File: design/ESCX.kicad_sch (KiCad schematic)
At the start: 18 parts, among them J1 HALL_ENC, J4 SWD, J5 USB_OTG, SW1 SENSOR_VOLTAGE

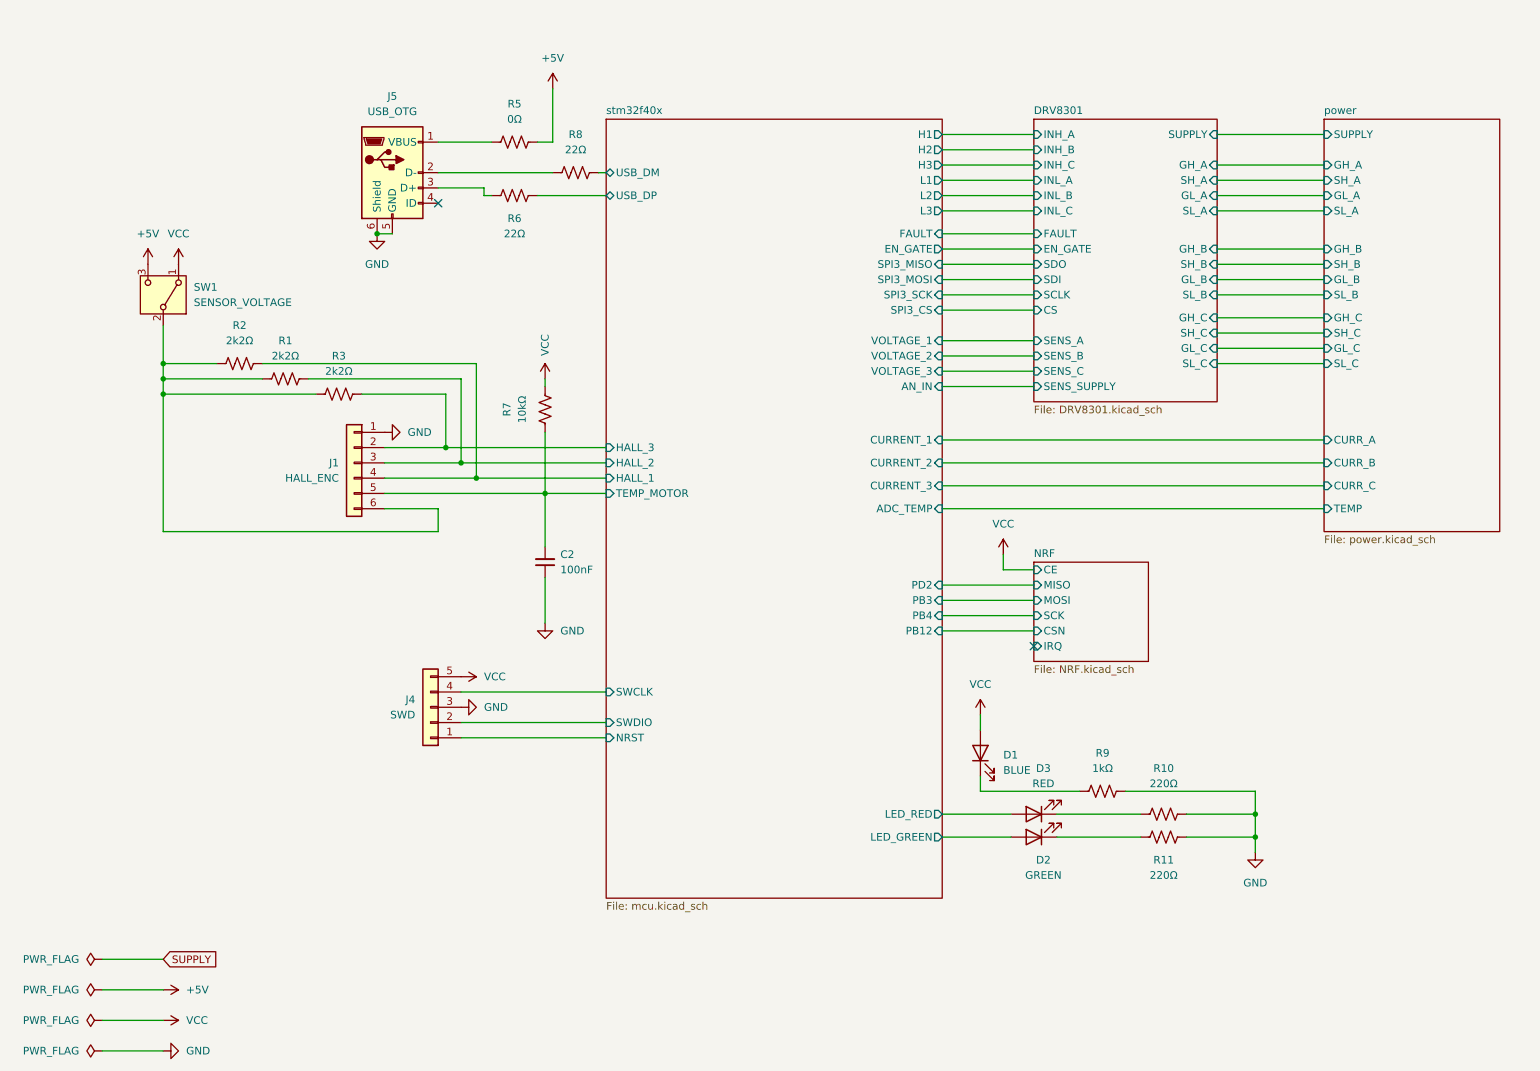
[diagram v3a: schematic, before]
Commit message: Cambios en el esquemático
- Cambio de Vcc por +3.3V
- Agregado de hoja para desarrollar la entrada de tensión alterna
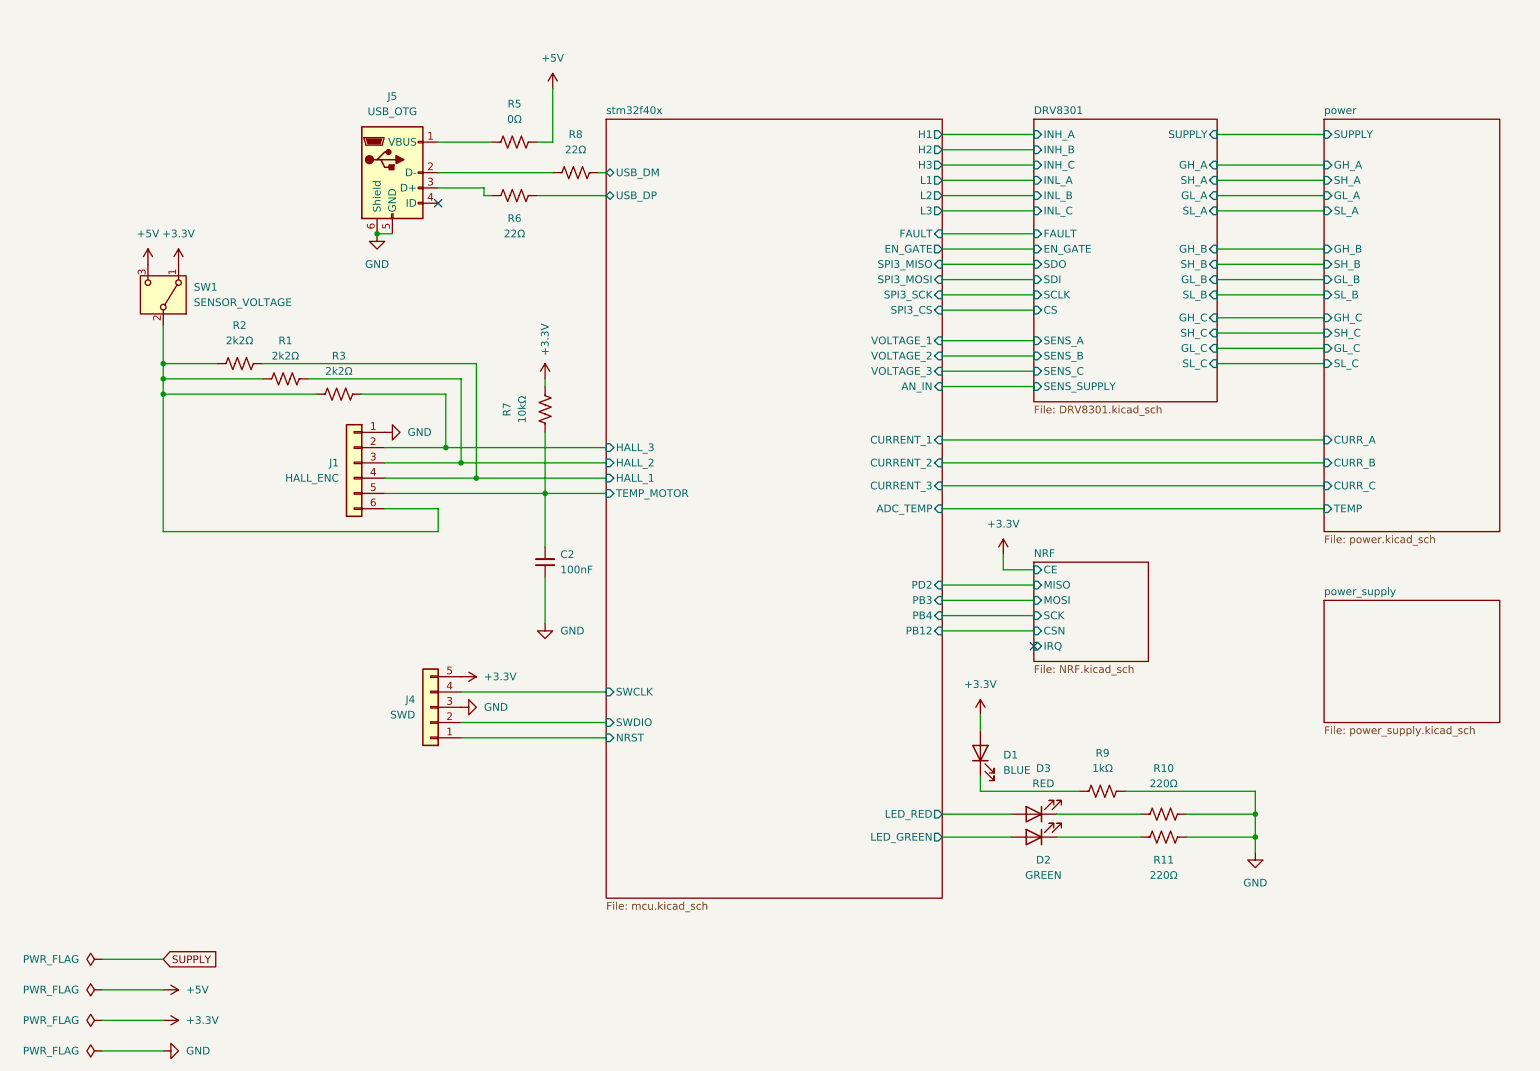
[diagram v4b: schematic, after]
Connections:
- net VCC renamed +3.3V
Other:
- added sheet power_supply (power_supply.kicad_sch)
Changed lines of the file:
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@@
 			)
 		)
-		(property "Value" "VCC"
+		(property "Value" "+3.3V"
 			(at 106.6799 72.39 90)
 			(effects
@@
 			)
 		)
-		(property "Value" "VCC"
+		(property "Value" "+3.3V"
 			(at 45.72 52.07 0)
 			(effects
@@
 			)
 		)
-		(property "Value" "VCC"
+		(property "Value" "+3.3V"
 			(at 46.99 182.8799 90)
 			(effects
@@
 			)
 		)
-		(property "Value" "VCC"
+		(property "Value" "+3.3V"
 			(at 96.52 125.7299 90)
 			(effects
@@
 			)
 		)
-		(property "Value" "VCC"
+		(property "Value" "+3.3V"
 			(at 179.07 127 0)
 			(effects
@@
 			)
 		)
-		(property "Value" "VCC"
+		(property "Value" "+3.3V"
 			(at 182.88 100.33 0)
 			(effects
@@
 				)
 			)
+		)
+	)
+	(sheet
+		(at 236.22 113.03)
+		(size 29.21 20.32)
+		(fields_autoplaced yes)
+		(stroke
+			(width 0.1524)
+			(type solid)
+		)
+		(fill
+			(color 0 0 0 0.0000)
+		)
+		(property "Sheetname" "power_supply"
+			(at 236.22 112.3184 0)
+			(effects
+				(font
+					(size 1.27 1.27)
+				)
+				(justify left bottom)
+			)
+		)
+		(property "Sheetfile" "power_supply.kicad_sch"
+			(at 236.22 133.9346 0)
+			(effects
+				(font
+					(size 1.27 1.27)
+				)
+				(justify left top)
+			)
+		)
+		(instances
+			(project "ESCX"
+				(path "/6389d757-a1bd-4c0a-9d55-6114b19cc67a"
+					(page "6")
+				)
+			)

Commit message: Commit antes del merge
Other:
- sheet DRV8301 ports: added none; removed SENS_A, SENS_B, SENS_C, SENS_SUPPLY
- sheet power ports: added SENS_A, SENS_B, SENS_C, SENS_SUPPLY; removed none
- sheet power_supply ports: added SUPPLY; removed none
